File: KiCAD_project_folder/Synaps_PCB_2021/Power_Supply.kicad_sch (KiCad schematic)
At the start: 30 parts, among them J1 USB_C_Receptacle, Q2 Q_PMOS_DGS, U1 MAX14748BEWW+

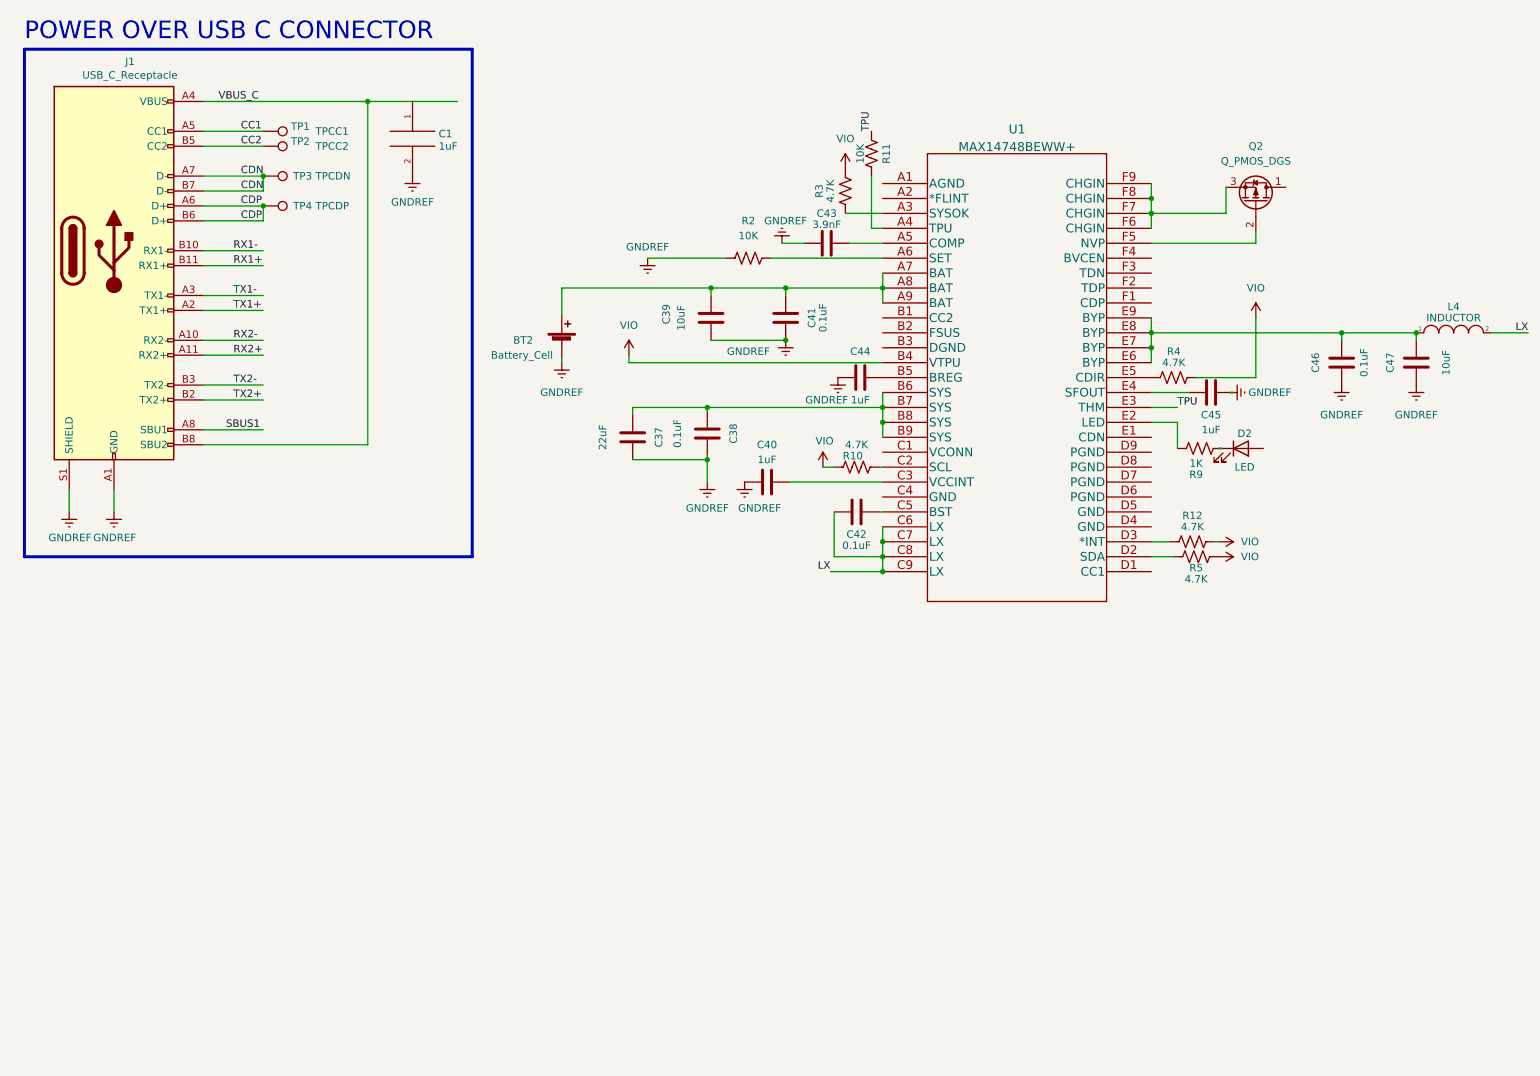
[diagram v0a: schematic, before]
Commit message: Reworking Powersupply
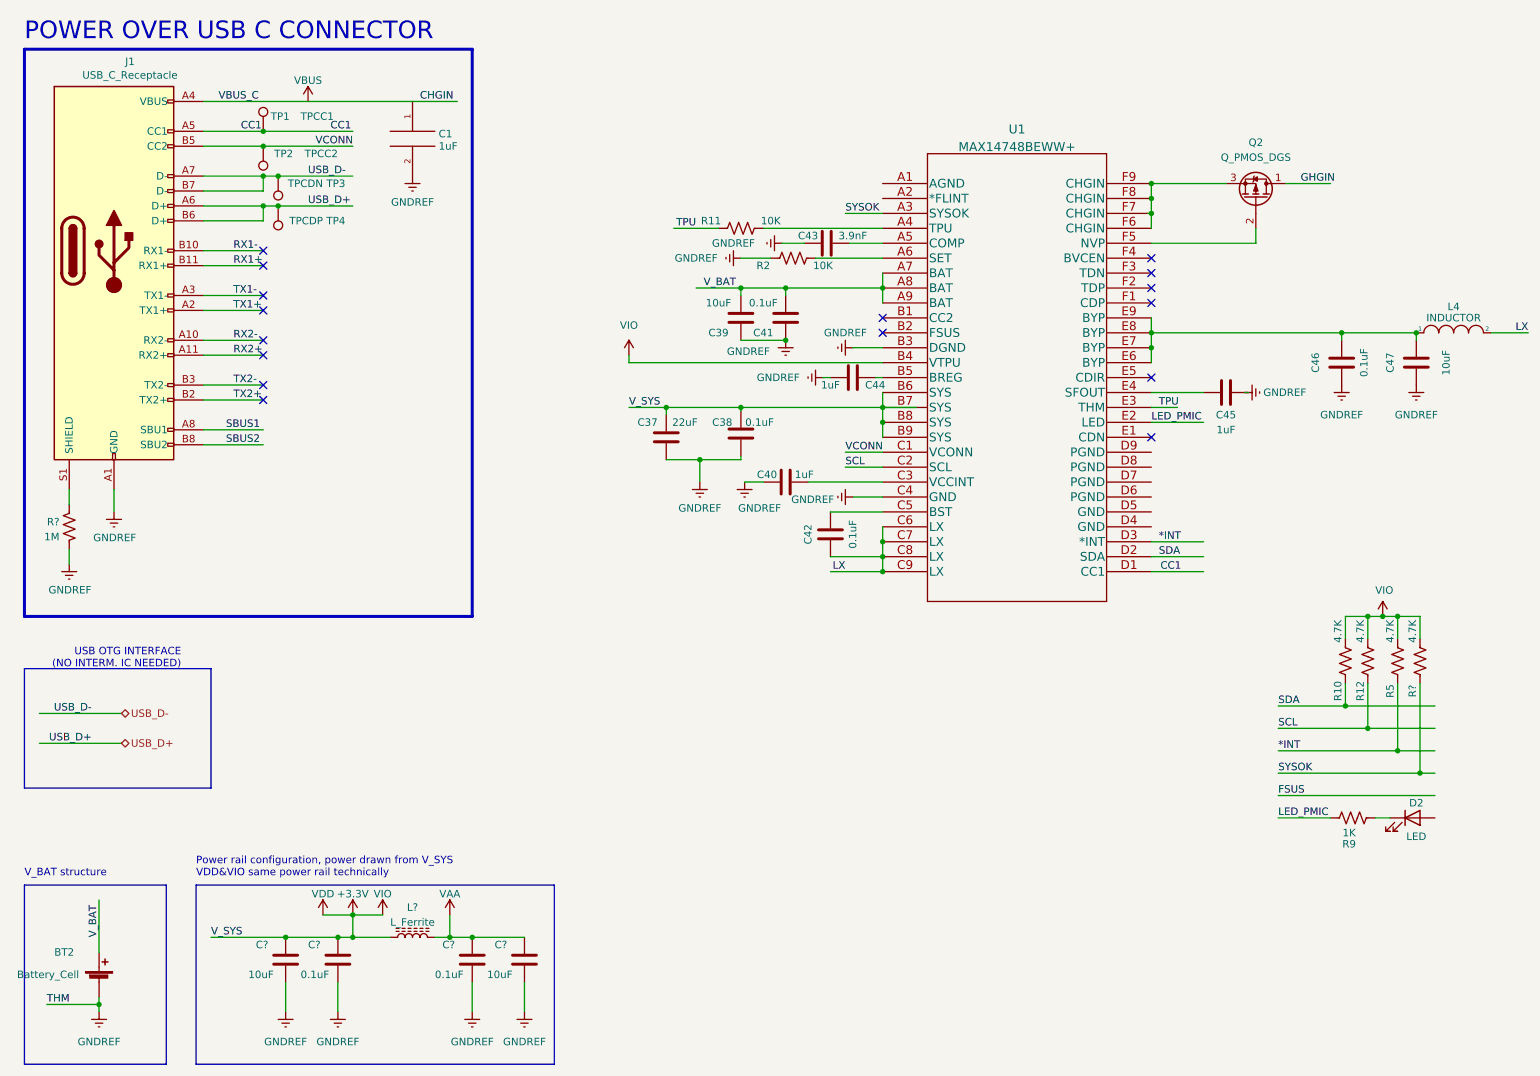
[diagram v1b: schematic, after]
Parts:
- removed R3, R4: 4.7K, Resistor_SMD:R_1206_3216Metric_Pad1.30x1.75mm_HandSolder, symbol Device:R_US
- added C? (x2): 0.1uF, symbol Device:C
- added C? (x2): 10uF, symbol Device:C
- added L?: L_Ferrite, symbol Device:L_Ferrite
- added R?: 1M, symbol Device:R_US
- added R?: 4.7K, Resistor_SMD:R_1206_3216Metric_Pad1.30x1.75mm_HandSolder, symbol Device:R_US
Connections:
- net CC2 is gone; now on net VCONN: J1.B5 (CC2), TP2.1
- net +1V1: now also C37.1, C38.1, R10.1, U1.B6 (SYS), U1.B7 (SYS), U1.B8 (SYS), U1.B9 (SYS), C?.1, C?.1, L?.1, R?.2; no longer R10.2
- net CC1: now also U1.D1 (CC1)
- net GNDREF: now also U1.B3 (DGND), U1.C4 (GND), C?.2, C?.2, C?.2, C?.2, R?.1; no longer J1.S1 (SHIELD)
- net SCL: now reaches U1.C2 (SCL)
- net SCL: now also R12.1; no longer R10.1
- net *INT: now reaches U1.D3 (*INT)
- net *INT: now also R5.1; no longer R12.1
- net V_BAT: now reaches BT2.1 (+), C39.1, C41.1, U1.A7 (BAT), U1.A8 (BAT), U1.A9 (BAT)
- net GHGIN: now reaches Q2.1 (D)
- net SYSOK: now reaches U1.A3 (SYSOK)
- net SYSOK: now also R?.1
- net VCONN: now reaches U1.C1 (VCONN)
- net SDA: now reaches U1.D2 (SDA)
- net SDA: now also R10.2; no longer R5.1
- net LED_PMIC: now reaches R9.1, U1.E2 (LED)
- net CDN renamed USB_D-
- net CDP renamed USB_D+
- net VBUS_C renamed CHGIN
- net CHGIN: no longer J1.B8 (SBU2)
- new net: J1.S1 (SHIELD), R?.2
- new net SBUS2: J1.B8 (SBU2)
- new net VAA: C?.1, C?.1, L?.2
- no-connect marks 0 -> 16
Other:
- note added: "Power rail configuration, power drawn from V_SYS VDD&VIO same power rail technically"
- note added: "USB OTG INTERFACE (NO INTERM. IC NEEDED)"
- note added: "V_BAT structure"
- moved on the sheet: BT2, C37, C38, C39, C40, C42, C44, C45, D2, Q2, R10, R11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

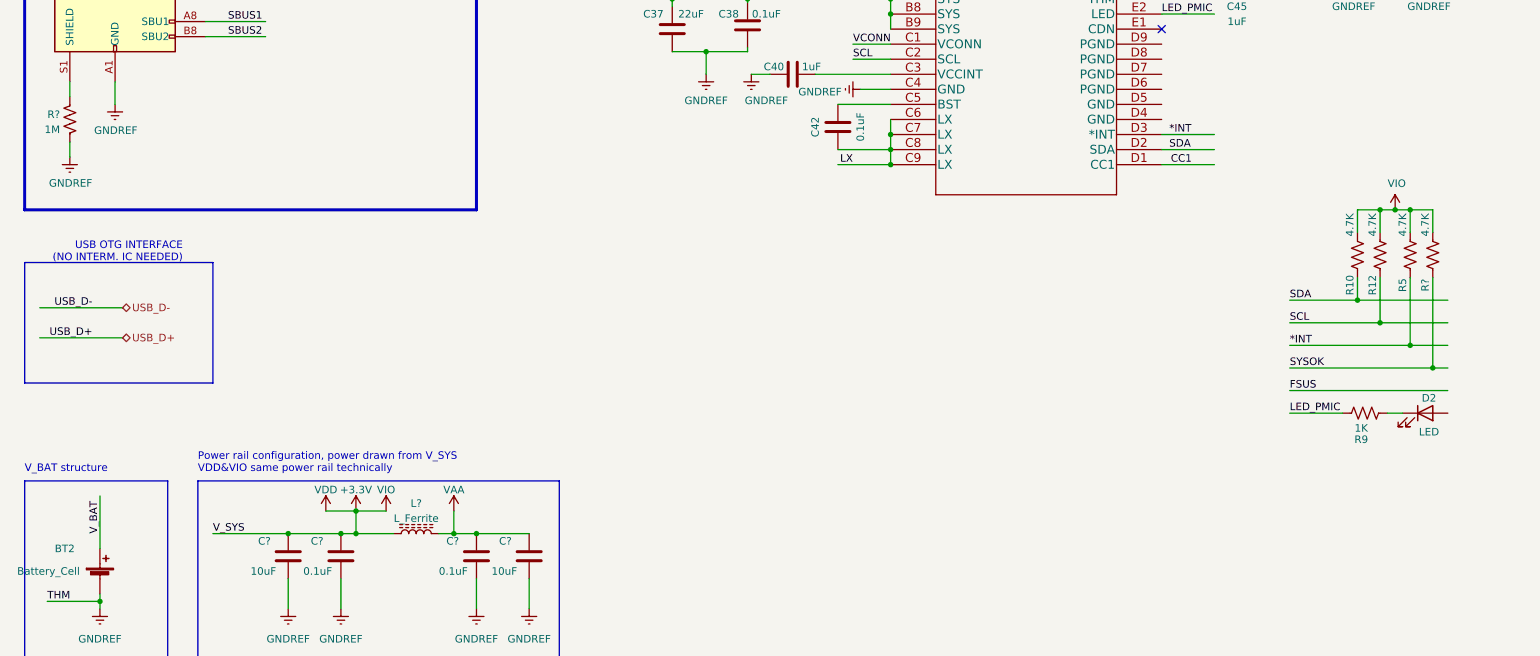
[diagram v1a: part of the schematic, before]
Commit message: updated missing annotation
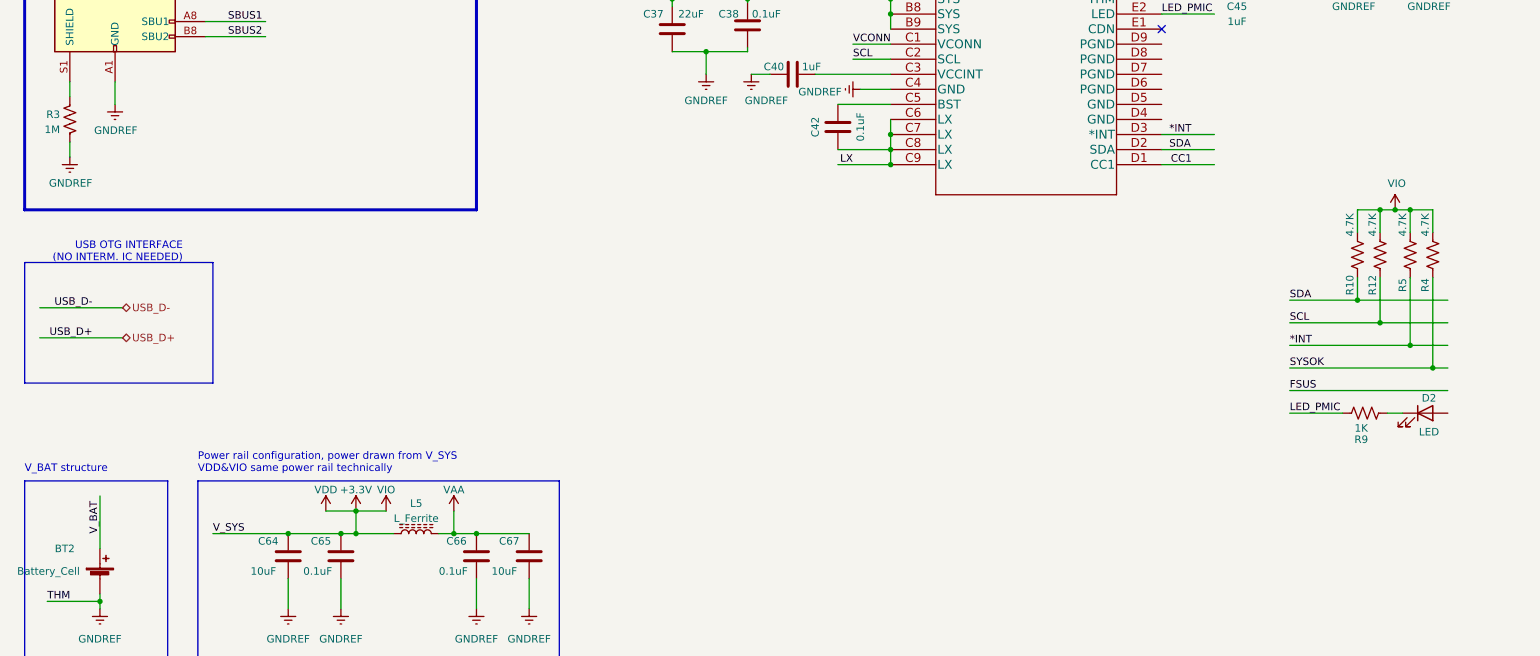
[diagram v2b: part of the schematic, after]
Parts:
- gave numbers to parts that had none: 7
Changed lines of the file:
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@@
   (symbol (lib_id "power:GNDREF") (at 63.5 184.15 0) (unit 1)
     (in_bom yes) (on_board yes) (fields_autoplaced)
-    (property "Reference" "#PWR?" (id 0) (at 63.5 190.5 0)
+    (property "Reference" "#PWR013" (id 0) (at 63.5 190.5 0)
       (effects (font (size 1.27 1.27)) hide)
     )
@@
   (symbol (lib_id "power:+3.3V") (at 74.93 167.64 0) (unit 1)
     (in_bom yes) (on_board yes) (fields_autoplaced)
-    (property "Reference" "#PWR?" (id 0) (at 74.93 171.45 0)
+    (property "Reference" "#PWR069" (id 0) (at 74.93 171.45 0)
       (effects (font (size 1.27 1.27)) hide)
     )
@@
   (symbol (lib_id "Device:R_US") (at 26.67 101.6 0) (mirror x) (unit 1)
     (in_bom yes) (on_board yes) (fields_autoplaced)
-    (property "Reference" "R?" (id 0) (at 25.019 100.7653 0)
+    (property "Reference" "R3" (id 0) (at 25.019 100.7653 0)
       (effects (font (size 1.27 1.27)) (justify right))
     )
@@
   (symbol (lib_id "power:GNDREF") (at 104.14 184.15 0) (unit 1)
     (in_bom yes) (on_board yes) (fields_autoplaced)
-    (property "Reference" "#PWR?" (id 0) (at 104.14 190.5 0)
+    (property "Reference" "#PWR073" (id 0) (at 104.14 190.5 0)
       (effects (font (size 1.27 1.27)) hide)
     )
@@
   (symbol (lib_id "power:GNDREF") (at 72.39 184.15 0) (unit 1)
     (in_bom yes) (on_board yes) (fields_autoplaced)
-    (property "Reference" "#PWR?" (id 0) (at 72.39 190.5 0)
+    (property "Reference" "#PWR068" (id 0) (at 72.39 190.5 0)
       (effects (font (size 1.27 1.27)) hide)
     )
@@
   (symbol (lib_id "power:GNDREF") (at 95.25 184.15 0) (unit 1)
     (in_bom yes) (on_board yes) (fields_autoplaced)
-    (property "Reference" "#PWR?" (id 0) (at 95.25 190.5 0)
+    (property "Reference" "#PWR072" (id 0) (at 95.25 190.5 0)
       (effects (font (size 1.27 1.27)) hide)
     )
@@
   (symbol (lib_id "power:VAA") (at 91.44 167.64 0) (unit 1)
     (in_bom yes) (on_board yes) (fields_autoplaced)
-    (property "Reference" "#PWR?" (id 0) (at 91.44 171.45 0)
+    (property "Reference" "#PWR071" (id 0) (at 91.44 171.45 0)
       (effects (font (size 1.27 1.27)) hide)
     )
@@
   (symbol (lib_id "power:GNDREF") (at 160.02 71.12 270) (unit 1)
     (in_bom yes) (on_board yes)
-    (property "Reference" "#PWR?" (id 0) (at 153.67 71.12 0)
+    (property "Reference" "#PWR074" (id 0) (at 153.67 71.12 0)
       (effects (font (size 1.27 1.27)) hide)
     )
@@
   (symbol (lib_id "Device:L_Ferrite") (at 85.09 171.45 90) (unit 1)
     (in_bom yes) (on_board yes) (fields_autoplaced)
-    (property "Reference" "L?" (id 0) (at 85.09 166.3532 90))
+    (property "Reference" "L5" (id 0) (at 85.09 166.3532 90))
     (property "Value" "L_Ferrite" (id 1) (at 85.09 168.8901 90))
     (property "Footprint" "" (id 2) (at 85.09 171.45 0)
@@
   (symbol (lib_id "Device:C") (at 95.25 175.26 0) (unit 1)
     (in_bom yes) (on_board yes)
-    (property "Reference" "C?" (id 0) (at 90.17 172.72 0)
+    (property "Reference" "C66" (id 0) (at 90.17 172.72 0)
       (effects (font (size 1.27 1.27)) (justify left))
     )
@@
   (symbol (lib_id "power:VDD") (at 69.85 167.64 0) (unit 1)
     (in_bom yes) (on_board yes) (fields_autoplaced)
-    (property "Reference" "#PWR?" (id 0) (at 69.85 171.45 0)
+    (property "Reference" "#PWR015" (id 0) (at 69.85 171.45 0)
       (effects (font (size 1.27 1.27)) hide)
     )
@@
   (symbol (lib_id "Device:C") (at 104.14 175.26 0) (unit 1)
     (in_bom yes) (on_board yes)
-    (property "Reference" "C?" (id 0) (at 99.06 172.72 0)
+    (property "Reference" "C67" (id 0) (at 99.06 172.72 0)
       (effects (font (size 1.27 1.27)) (justify left))
     )
@@
   (symbol (lib_id "power:GNDREF") (at 160.02 96.52 270) (unit 1)
     (in_bom yes) (on_board yes) (fields_autoplaced)
-    (property "Reference" "#PWR?" (id 0) (at 153.67 96.52 0)
+    (property "Reference" "#PWR075" (id 0) (at 153.67 96.52 0)
       (effects (font (size 1.27 1.27)) hide)
     )
@@
   (symbol (lib_id "Device:R_US") (at 256.54 124.46 180) (unit 1)
     (in_bom yes) (on_board yes)
-    (property "Reference" "R?" (id 0) (at 255.27 129.54 90))
+    (property "Reference" "R4" (id 0) (at 255.27 129.54 90))
     (property "Value" "4.7K" (id 1) (at 255.27 119.38 90))
     (property "Footprint" "Resistor_SMD:R_1206_3216Metric_Pad1.30x1.75mm_HandSolder" (id 2) (at 255.524 124.206 90)
@@
   (symbol (lib_id "Device:C") (at 72.39 175.26 0) (unit 1)
     (in_bom yes) (on_board yes)
-    (property "Reference" "C?" (id 0) (at 67.31 172.72 0)
+    (property "Reference" "C65" (id 0) (at 67.31 172.72 0)
       (effects (font (size 1.27 1.27)) (justify left))
     )
@@
   (symbol (lib_id "project_library_MICSAPCB:VIO") (at 80.01 167.64 0) (unit 1)
     (in_bom yes) (on_board yes) (fields_autoplaced)
-    (property "Reference" "#PWR?" (id 0) (at 80.01 171.45 0)
+    (property "Reference" "#PWR070" (id 0) (at 80.01 171.45 0)
       (effects (font (size 1.27 1.27)) hide)
     )
@@
   (symbol (lib_id "power:VBUS") (at 67.31 29.21 0) (unit 1)
     (in_bom yes) (on_board yes) (fields_autoplaced)
-    (property "Reference" "#PWR?" (id 0) (at 67.31 33.02 0)
+    (property "Reference" "#PWR014" (id 0) (at 67.31 33.02 0)
       (effects (font (size 1.27 1.27)) hide)
     )
@@
   (symbol (lib_id "Device:C") (at 63.5 175.26 0) (unit 1)
     (in_bom yes) (on_board yes)
-    (property "Reference" "C?" (id 0) (at 58.42 172.72 0)
-      (effects (font (size 1.27 1.27)) (justify left))
-    )
+    (property "Reference" "C64" (id 0) (at 58.42 172.72 0)
+      (effects (font (size 1.27 1.27)) (justify left))
+    )
